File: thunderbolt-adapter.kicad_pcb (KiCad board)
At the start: 6 copper layers, 165 x 30 mm, 98 parts, among them J4 E8124-015-01, J5 PCIe_x16_10146070-113Y0LF-ver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, J6 Molex_1724480008-horizontal, J7 BarrelJack_3167288, Q2 BC817-25W, Q3 DZDH0401DW, Q4 DZDH0401DW, Q5 SI7613DN-T1-GE3, Q6 SI7613DN-T1-GE3, U1 LT8350RV#PBF, U2 MP2386GG, U3 TPS65983BAZBHR, U4 JHL6340SLLSQ, U5 MX25L8006EM1I-12G

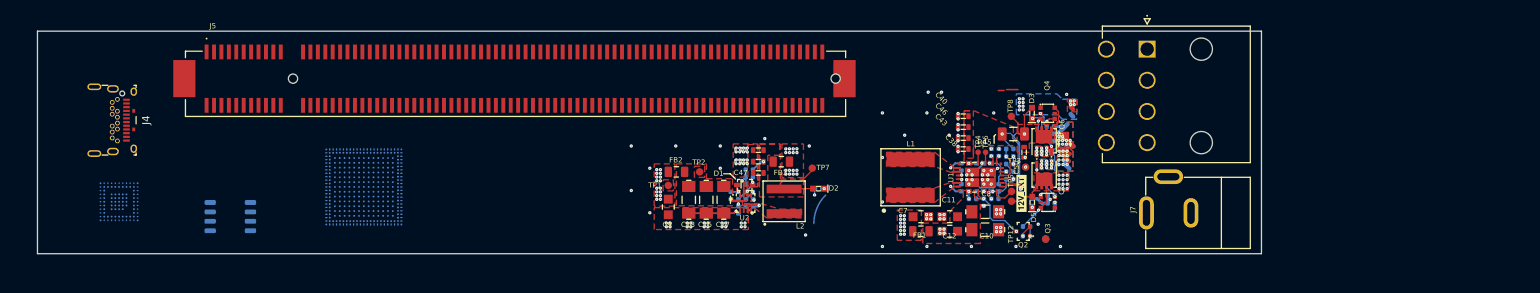
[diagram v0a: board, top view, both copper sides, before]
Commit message: Updated mechanical mockup
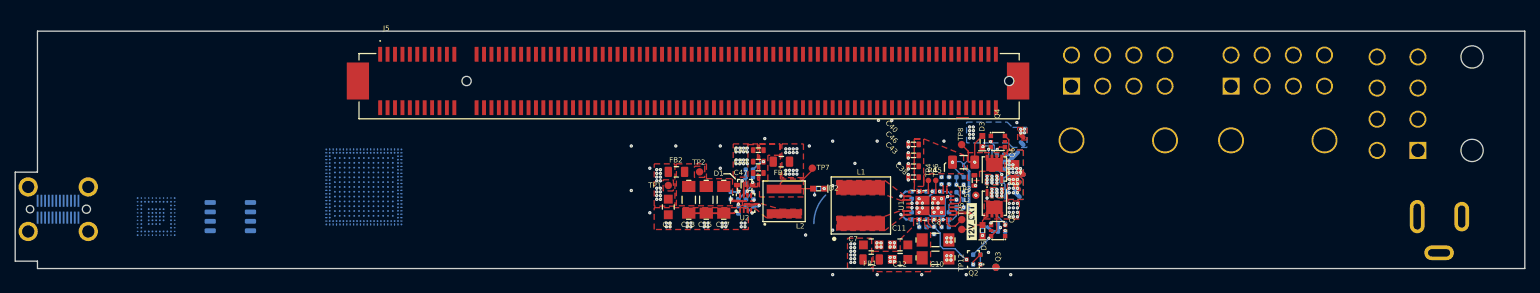
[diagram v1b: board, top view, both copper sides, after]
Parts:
- removed J4: E8124-015-01, antmicro-footprints:USB-C_Female_E8124-015-01
- added J**: KUSBXSL2CS1N24BTR, antmicro-footprints:KUSBXSL2CS1N24BTR, B.Cu at (79.0, 134.0)
- added J1: 455860005, antmicro-footprints:MOLEX_455860005, B.Cu at (219.4, 117.4)
- added J2: 455860005, antmicro-footprints:MOLEX_455860005, B.Cu at (240.9, 117.4)
- J6, J7: moved to B.Cu
- moved J6 39.0 mm to (266.1, 126.1), turned to -90 degrees
- moved J7 36.5 mm to (266.0, 135.0), turned to -90 degrees
- moved J5 23.4 mm to (167.7, 117.2)
- moved C1 7.71 mm to (211.8, 129.0)
- moved C11 7.71 mm to (196.3, 138.8)
- moved C12 7.71 mm to (196.3, 140.8)
- moved C19 7.71 mm to (202.9, 130.2)
- moved C40 7.71 mm to (198.1, 125.3)
- moved C43 7.71 mm to (198.1, 128.2)
- moved C6 7.71 mm to (211.8, 129.0)
- moved C7 7.71 mm to (192.4, 138.8)
- moved FB1 7.71 mm to (192.4, 140.8)
- moved L1 7.71 mm to (191.0, 133.5)
- moved Q3 7.71 mm to (209.5, 136.9)
- moved R24 7.71 mm to (201.9, 132.1)
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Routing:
- net unconnected-(J1-Pad1): track 0.00 -> 4.25 mm, vias 0 -> 1
- net /TB Controller/PA_AUX_P: track 4.25 -> 0.00 mm
- net unconnected-(J1-Pad3): track 0.00 -> 2.48 mm, vias 0 -> 1
- net PCIE_CLK_CON_P: track 2.38 -> 0.00 mm
- net unconnected-(J2-Pad2): track 0.00 -> 0.94 mm, vias 0 -> 5
- net 3V3_SYS: track 1.43 -> 0.49 mm, vias 28 -> 24
- net Net-(C114-Pad2): track 0.10 -> 0.00 mm, vias 1 -> 0
- net GND: vias 125 -> 95
- net unconnected-(J5-PadB82): vias 0 -> 1
- net unconnected-(J5-PadB73): vias 0 -> 1
- net unconnected-(J5-PadB67): vias 0 -> 1
- net unconnected-(J2-PadS2): vias 0 -> 1
- net unconnected-(J2-PadS1): vias 0 -> 8
- net unconnected-(J2-Pad7): vias 0 -> 1
- net unconnected-(J2-Pad3): vias 0 -> 1
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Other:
- board size 165 x 30 mm -> 203.5 x 32 mm

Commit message: Sch - connected power connectors and USB C
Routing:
- net unconnected-(J2-PadS1): vias 8 -> 0
- net unconnected-(J1-PadS2): vias 14 -> 1
- net GND: vias 95 -> 116
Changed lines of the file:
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@@
     (property "Tolerance" "1%")
     (property "Val" "100k")
-    (attr exclude_from_pos_files)
+    (attr exclude_from_pos_files exclude_from_bom)
     (fp_text reference "R24" (at -1.065 -5.555 90) (layer "B.SilkS")
       (effects (font (size 0.7 0.7) (thickness 0.15)) (justify right bottom mirror))
@@
   (via (at 197.4 127.104998) (size 0.45) (drill 0.1) (layers "F.Cu" "B.Cu") (net 1))
   (via (at 183.55 137.48) (size 0.45) (drill 0.1) (layers "F.Cu" "B.Cu") (net 1))
+  (via (at 174.180001 127.87) (size 0.45) (drill 0.1) (layers "F.Cu" "B.Cu") (net 1))
+  (via (at 167.580001 136.37) (size 0.45) (drill 0.1) (layers "F.Cu" "B.Cu") (net 1))
   (via (at 201.4025 133.175) (size 0.45) (drill 0.1) (layers "F.Cu" "B.Cu") (net 1))
+  (via (at 175.680001 126.27) (size 0.45) (drill 0.1) (layers "F.Cu" "B.Cu") (net 1))
   (via (at 195.5125 140.49) (size 0.45) (drill 0.1) (layers "F.Cu" "B.Cu") (net 1))
   (via (at 206.140001 141.435) (size 0.45) (drill 0.1) (layers "F.Cu" "B.Cu") (net 1))
@@
   (via (at 175.380001 135.87) (size 0.45) (drill 0.1) (layers "F.Cu" "B.Cu") (net 1))
   (via (at 160.05 125.48) (size 0.45) (drill 0.1) (layers "F.Cu" "B.Cu") (net 1))
+  (via (at 169.880001 135.87) (size 0.45) (drill 0.1) (layers "F.Cu" "B.Cu") (net 1))
+  (via (at 175.180001 126.27) (size 0.45) (drill 0.1) (layers "F.Cu" "B.Cu") (net 1))
   (via (at 198.85 134.426) (size 0.45) (drill 0.1) (layers "F.Cu" "B.Cu") (net 1))
+  (via (at 174.680001 127.37) (size 0.45) (drill 0.1) (layers "F.Cu" "B.Cu") (net 1))
   (via (at 194.9525 138.53) (size 0.45) (drill 0.1) (layers "F.Cu" "B.Cu") (net 1))
   (via (at 172.280001 135.87) (size 0.45) (drill 0.1) (layers "F.Cu" "B.Cu") (net 1))
@@
   (via (at 204.855 130.7) (size 0.45) (drill 0.1) (layers "F.Cu" "B.Cu") (net 1))
   (via (at 164.780001 135.87) (size 0.45) (drill 0.1) (layers "F.Cu" "B.Cu") (net 1))
+  (via (at 170.380001 135.87) (size 0.45) (drill 0.1) (layers "F.Cu" "B.Cu") (net 1))
   (via (at 197.4 130.054997) (size 0.45) (drill 0.1) (layers "F.Cu" "B.Cu") (net 1))
   (via (at 212 129.035) (size 0.45) (drill 0.1) (layers "F.Cu" "B.Cu") (net 1))
@@
   (via (at 203.14 140.28) (size 0.45) (drill 0.1) (layers "F.Cu" "B.Cu") (net 1))
   (via (at 199.2925 133.175) (size 0.45) (drill 0.1) (layers "F.Cu" "B.Cu") (net 1))
+  (via (at 175.180001 127.37) (size 0.45) (drill 0.1) (layers "F.Cu" "B.Cu") (net 1))
   (via (at 202.58 137.87) (size 0.45) (drill 0.1) (layers "F.Cu" "B.Cu") (net 1))
   (via (at 172.280001 136.37) (size 0.45) (drill 0.1) (layers "F.Cu" "B.Cu") (net 1))
+  (via (at 174.180001 126.27) (size 0.45) (drill 0.1) (layers "F.Cu" "B.Cu") (net 1))
   (via (at 172.780001 136.37) (size 0.45) (drill 0.1) (layers "F.Cu" "B.Cu") (net 1))
   (via (at 195.5125 141.05) (size 0.45) (drill 0.1) (layers "F.Cu" "B.Cu") (net 1))
   (via (at 201.87 134.426) (size 0.45) (drill 0.1) (layers "F.Cu" "B.Cu") (net 1))
   (via (at 212 128.525001) (size 0.45) (drill 0.1) (layers "F.Cu" "B.Cu") (net 1))
+  (via (at 168.080001 136.37) (size 0.45) (drill 0.1) (layers "F.Cu" "B.Cu") (net 1))
   (via (at 211.49 128.015002) (size 0.45) (drill 0.1) (layers "F.Cu" "B.Cu") (net 1))
   (via (at 164.780001 136.37) (size 0.45) (drill 0.1) (layers "F.Cu" "B.Cu") (net 1))
@@
   (via (at 184.762 132.08) (size 0.45) (drill 0.1) (layers "F.Cu" "B.Cu") (net 1))
   (via (at 193.72 138.535) (size 0.45) (drill 0.1) (layers "F.Cu" "B.Cu") (net 1))
+  (via (at 167.580001 135.87) (size 0.45) (drill 0.1) (layers "F.Cu" "B.Cu") (net 1))
   (via (at 202.58 138.43) (size 0.45) (drill 0.1) (layers "F.Cu" "B.Cu") (net 1))
   (via (at 202.58 140.84) (size 0.45) (drill 0.1) (layers "F.Cu" "B.Cu") (net 1))
   (via (at 211.49 129.035) (size 0.45) (drill 0.1) (layers "F.Cu" "B.Cu") (net 1))
   (via (at 175.180001 127.87) (size 0.45) (drill 0.1) (layers "F.Cu" "B.Cu") (net 1))
+  (via (at 174.680001 126.27) (size 0.45) (drill 0.1) (layers "F.Cu" "B.Cu") (net 1))
   (via (at 172.780001 135.87) (size 0.45) (drill 0.1) (layers "F.Cu" "B.Cu") (net 1))
+  (via (at 168.080001 135.87) (size 0.45) (drill 0.1) (layers "F.Cu" "B.Cu") (net 1))
   (via (at 204.854 131.71) (size 0.45) (drill 0.1) (layers "F.Cu" "B.Cu") (net 1))
   (via (at 165.280001 136.37) (size 0.45) (drill 0.1) (layers "F.Cu" "B.Cu") (net 1))
@@
   (via (at 200.860001 137.355) (size 0.45) (drill 0.1) (layers "F.Cu" "B.Cu") (net 1))
   (via (at 202.58 140.28) (size 0.45) (drill 0.1) (layers "F.Cu" "B.Cu") (net 1))
+  (via (at 174.180001 127.37) (size 0.45) (drill 0.1) (layers "F.Cu" "B.Cu") (net 1))
   (via (at 202.89 129.666) (size 0.45) (drill 0.1) (layers "F.Cu" "B.Cu") (net 1))
   (via (at 199.2 142.825) (size 0.45) (drill 0.1) (layers "F.Cu" "B.Cu") (net 1))
+  (via (at 169.880001 136.37) (size 0.45) (drill 0.1) (layers "F.Cu" "B.Cu") (net 1))
   (via (at 210.98 129.035) (size 0.45) (drill 0.1) (layers "F.Cu" "B.Cu") (net 1))
+  (via (at 174.680001 125.77) (size 0.45) (drill 0.1) (layers "F.Cu" "B.Cu") (net 1))
   (via (at 175.380001 136.37) (size 0.45) (drill 0.1) (layers "F.Cu" "B.Cu") (net 1))
   (via (at 175.709001 131.575) (size 0.45) (drill 0.1) (layers "F.Cu" "B.Cu") (net 1))
@@
   (via (at 197.4 129.325) (size 0.45) (drill 0.1) (layers "F.Cu" "B.Cu") (net 1))
   (via (at 187.2 142.825) (size 0.45) (drill 0.1) (layers "F.Cu" "B.Cu") (net 1))
+  (via (at 175.680001 125.77) (size 0.45) (drill 0.1) (layers "F.Cu" "B.Cu") (net 1))
   (via (at 208.2 139.825) (size 0.45) (drill 0.1) (layers "F.Cu" "B.Cu") (net 1))
   (via (at 200.87 132.584) (size 0.45) (drill 0.1) (layers "F.Cu" "B.Cu") (net 1))
   (via (at 197.4 124.9) (size 0.45) (drill 0.1) (layers "F.Cu" "B.Cu") (net 1))
   (via (at 210.98 127.505003) (size 0.45) (drill 0.1) (layers "F.Cu" "B.Cu") (net 1))
+  (via (at 170.380001 136.37) (size 0.45) (drill 0.1) (layers "F.Cu" "B.Cu") (net 1))
   (via (at 174.880001 136.37) (size 0.45) (drill 0.1) (layers "F.Cu" "B.Cu") (net 1))
   (via (at 197.4 125.629997) (size 0.45) (drill 0.1) (layers "F.Cu" "B.Cu") (net 1))
@@
   (via (at 200.87 134.426) (size 0.45) (drill 0.1) (layers "F.Cu" "B.Cu") (net 1))
   (via (at 203.14 138.43) (size 0.45) (drill 0.1) (layers "F.Cu" "B.Cu") (net 1))
+  (via (at 175.180001 125.77) (size 0.45) (drill 0.1) (layers "F.Cu" "B.Cu") (net 1))
+  (via (at 174.680001 127.87) (size 0.45) (drill 0.1) (layers "F.Cu" "B.Cu") (net 1))
   (via (at 175.680001 127.37) (size 0.45) (drill 0.1) (layers "F.Cu" "B.Cu") (net 1))
   (via (at 199.2925 133.825) (size 0.45) (drill 0.1) (layers "F.Cu" "B.Cu") (net 1))
@@
   (via (at 212.51 129.035) (size 0.45) (drill 0.1) (layers "F.Cu" "B.Cu") (net 1))
   (via (at 194.9525 139.09) (size 0.45) (drill 0.1) (layers "F.Cu" "B.Cu") (net 1))
+  (via (at 174.180001 125.77) (size 0.45) (drill 0.1) (layers "F.Cu" "B.Cu") (net 1))
   (segment (start 174.490001 132.64) (end 174.521002 132.64) (width 0.25) (layer "B.Cu") (net 1))
   (segment (start 175.709001 131.421) (end 176.445001 130.685) (width 0.25) (layer "B.Cu") (net 1))
@@
   (via (at 195.17 122.026) (size 0.45) (drill 0.1) (layers "F.Cu" "B.Cu") (net 405))
   (via (at 211.2 142.825) (size 0.45) (drill 0.1) (layers "F.Cu" "B.Cu") (net 411))
-  (via (at 174.180001 127.87) (size 0.45) (drill 0.1) (layers "F.Cu" "B.Cu") (net 412))
-  (via (at 175.680001 126.27) (size 0.45) (drill 0.1) (layers "F.Cu" "B.Cu") (net 412))
-  (via (at 175.180001 126.27) (size 0.45) (drill 0.1) (layers "F.Cu" "B.Cu") (net 412))
-  (via (at 174.680001 127.37) (size 0.45) (drill 0.1) (layers "F.Cu" "B.Cu") (net 412))
-  (via (at 175.180001 127.37) (size 0.45) (drill 0.1) (layers "F.Cu" "B.Cu") (net 412))
-  (via (at 174.180001 126.27) (size 0.45) (drill 0.1) (layers "F.Cu" "B.Cu") (net 412))
-  (via (at 174.680001 126.27) (size 0.45) (drill 0.1) (layers "F.Cu" "B.Cu") (net 412))
-  (via (at 174.180001 127.37) (size 0.45) (drill 0.1) (layers "F.Cu" "B.Cu") (net 412))
-  (via (at 174.680001 125.77) (size 0.45) (drill 0.1) (layers "F.Cu" "B.Cu") (net 412))
-  (via (at 175.680001 125.77) (size 0.45) (drill 0.1) (layers "F.Cu" "B.Cu") (net 412))
-  (via (at 175.180001 125.77) (size 0.45) (drill 0.1) (layers "F.Cu" "B.Cu") (net 412))
-  (via (at 174.680001 127.87) (size 0.45) (drill 0.1) (layers "F.Cu" "B.Cu") (net 412))
   (via (at 172.05 125.48) (size 0.45) (drill 0.1) (layers "F.Cu" "B.Cu") (net 412))
-  (via (at 174.180001 125.77) (size 0.45) (drill 0.1) (layers "F.Cu" "B.Cu") (net 412))
   (segment (start 212.71 123.325) (end 212.55 123.485) (width 0.6) (layer "F.Cu") (net 414))
   (segment (start 212.907046 124.325) (end 212.562801 123.980755) (width 0.6) (layer "F.Cu") (net 414))
@@
   (via (at 162.55 128.48) (size 0.45) (drill 0.1) (layers "F.Cu" "B.Cu") (net 415))
   (via (at 193.2 142.825) (size 0.45) (drill 0.1) (layers "F.Cu" "B.Cu") (net 419))
-  (via (at 167.580001 136.37) (size 0.45) (drill 0.1) (layers "F.Cu" "B.Cu") (net 421))
-  (via (at 169.880001 135.87) (size 0.45) (drill 0.1) (layers "F.Cu" "B.Cu") (net 421))
-  (via (at 170.380001 135.87) (size 0.45) (drill 0.1) (layers "F.Cu" "B.Cu") (net 421))
-  (via (at 168.080001 136.37) (size 0.45) (drill 0.1) (layers "F.Cu" "B.Cu") (net 421))
-  (via (at 167.580001 135.87) (size 0.45) (drill 0.1) (layers "F.Cu" "B.Cu") (net 421))
-  (via (at 168.080001 135.87) (size 0.45) (drill 0.1) (layers "F.Cu" "B.Cu") (net 421))
-  (via (at 169.880001 136.37) (size 0.45) (drill 0.1) (layers "F.Cu" "B.Cu") (net 421))
-  (via (at 170.380001 136.37) (size 0.45) (drill 0.1) (layers "F.Cu" "B.Cu") (net 421))
   (via (at 187.2 130.825) (size 0.45) (drill 0.1) (layers "F.Cu" "B.Cu") (net 422))
   (zone (net 4) (net_name "Net-(C26-Pad2)") (layer "F.Cu") (hatch edge 0.508)
